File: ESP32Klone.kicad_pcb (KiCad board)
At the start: 2 copper layers, 52.1 x 65.5 mm, 23 parts, among them J1 USB_C_Receptacle_USB2.0_14P, J2 Conn_01x14_Socket, J3 Conn_01x14_Socket, U1 CH340G, U2 AMS1117-3.3, U3 ESP32-WROOM-32E, X1 12MHz

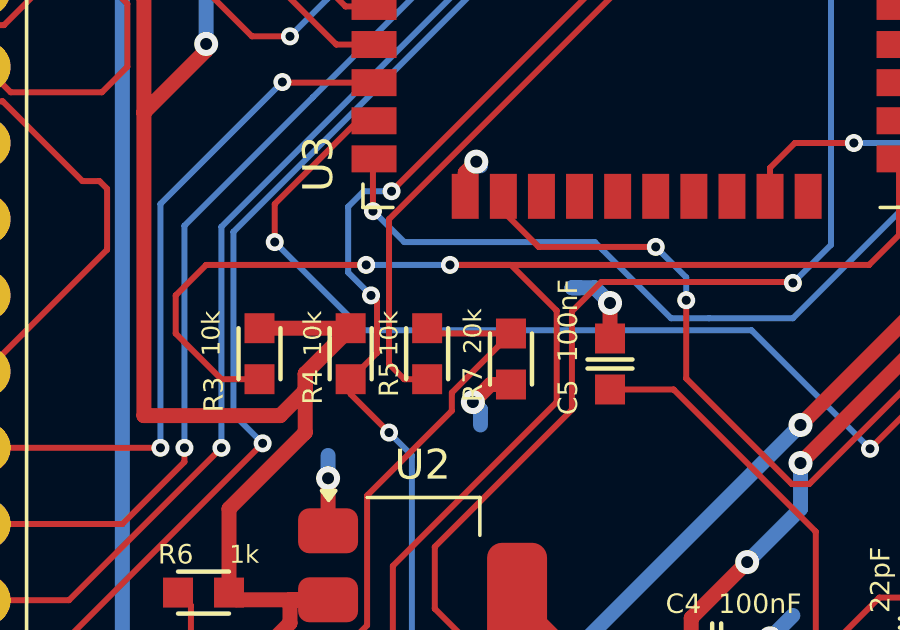
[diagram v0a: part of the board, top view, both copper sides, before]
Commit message: fix: correct UART Rx level shifter wiring (R5/R7)
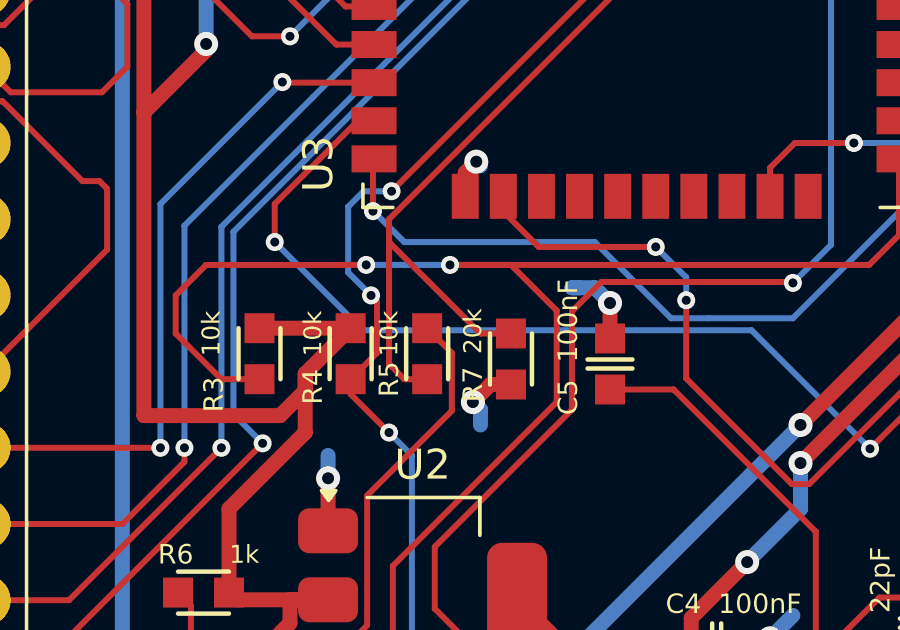
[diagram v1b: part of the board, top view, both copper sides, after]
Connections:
- R7 pad 1: /TXD/RXD -> Net-(U3-RXD0/IO3)
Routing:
- net Net-(U3-RXD0/IO3): track 28.9 -> 34.2 mm
- net /TXD/RXD: track 80.5 -> 77.3 mm
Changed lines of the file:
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@@
 			(size 1 1)
 			(layers "F.Cu" "F.Mask" "F.Paste")
-			(net 39 "/TXD{slash}RXD")
+			(net 38 "Net-(U3-RXD0{slash}IO3)")
 			(pintype "passive")
 		)
@@
 	)
 	(segment
+		(start 141.732 106.934)
+		(end 140.716 106.934)
+		(width 0.2)
+		(layer "F.Cu")
+		(net 38)
+	)
+	(segment
 		(start 145.542 95.25)
 		(end 147.574 95.25)
@@
 	)
 	(segment
+		(start 137.668 107.95)
+		(end 137.668 103.886)
+		(width 0.2)
+		(layer "F.Cu")
+		(net 38)
+	)
+	(segment
 		(start 138.176 108.458)
 		(end 137.668 107.95)
@@
 	)
 	(segment
-		(start 137.668 107.95)
-		(end 137.668 103.124)
+		(start 140.716 106.934)
+		(end 137.668 103.886)
 		(width 0.2)
 		(layer "F.Cu")
@@
 	)
 	(segment
-		(start 147.574 95.25)
-		(end 153.142 89.682)
+		(start 137.668 103.886)
+		(end 137.668 103.124)
 		(width 0.2)
 		(layer "F.Cu")
@@
 	)
 	(segment
-		(start 153.269 126.731968)
-		(end 153.269 126.445101)
+		(start 147.574 95.25)
+		(end 153.142 89.682)
 		(width 0.2)
 		(layer "F.Cu")
-		(net 39)
+		(net 38)
 	)
 	(segment
-		(start 151.476968 128.524)
-		(end 153.269 126.731968)
+		(start 136.974215 136.291)
+		(end 134.335 133.651785)
 		(width 0.2)
 		(layer "F.Cu")
@@
 	)
 	(segment
-		(start 149.854 123.103032)
-		(end 150.114032 122.843)
+		(start 154.833 134.7861)
+		(end 153.3281 136.291)
 		(width 0.2)
 		(layer "F.Cu")
@@
 	)
 	(segment
-		(start 153.3281 136.291)
-		(end 136.974215 136.291)
+		(start 154.833 125.530032)
+		(end 154.833 134.7861)
 		(width 0.2)
 		(layer "F.Cu")
@@
 	)
 	(segment
-		(start 150.114032 122.843)
-		(end 152.145968 122.843)
+		(start 153.269 126.731968)
+		(end 153.269 126.445101)
 		(width 0.2)
 		(layer "F.Cu")
@@
 	)
 	(segment
-		(start 136.937 112.334364)
-		(end 139.761 109.510364)
+		(start 136.937 116.663008)
+		(end 136.937 112.334364)
 		(width 0.2)
 		(layer "F.Cu")
@@
 	)
 	(segment
-		(start 139.761 108.905)
-		(end 141.732 106.934)
+		(start 152.145968 122.843)
+		(end 154.833 125.530032)
 		(width 0.2)
 		(layer "F.Cu")
@@
 	)
 	(segment
-		(start 136.937 116.663008)
-		(end 136.937 112.334364)
+		(start 150.114032 122.843)
+		(end 152.145968 122.843)
 		(width 0.2)
 		(layer "F.Cu")
@@
 	)
 	(segment
-		(start 139.761 109.510364)
-		(end 139.761 108.905)
+		(start 149.854 123.103032)
+		(end 150.114032 122.843)
 		(width 0.2)
 		(layer "F.Cu")
@@
 	)
 	(segment
-		(start 149.854 125.054968)
-		(end 149.854 123.103032)
+		(start 152.138899 125.315)
+		(end 150.114032 125.315)
 		(width 0.2)
 		(layer "F.Cu")
@@
 	)
 	(segment
-		(start 134.335 117.454992)
-		(end 134.730992 117.059)
+		(start 139.761 107.581)
+		(end 138.938 106.758)
 		(width 0.2)
 		(layer "F.Cu")
@@
 	)
 	(segment
-		(start 151.13 128.524)
-		(end 151.476968 128.524)
+		(start 149.854 125.054968)
+		(end 149.854 123.103032)
 		(width 0.2)
 		(layer "F.Cu")
@@
 	)
 	(segment
-		(start 152.138899 125.315)
-		(end 150.114032 125.315)
+		(start 134.335 133.651785)
+		(end 134.335 117.454992)
 		(width 0.2)
 		(layer "F.Cu")
@@
 	)
 	(segment
-		(start 154.833 125.530032)
-		(end 154.833 134.7861)
+		(start 136.937 112.334364)
+		(end 139.761 109.510364)
 		(width 0.2)
 		(layer "F.Cu")
@@
 	)
 	(segment
-		(start 141.732 106.934)
-		(end 139.114 106.934)
+		(start 151.476968 128.524)
+		(end 153.269 126.731968)
 		(width 0.2)
 		(layer "F.Cu")
@@
 	)
 	(segment
-		(start 154.833 134.7861)
-		(end 153.3281 136.291)
+		(start 153.3281 136.291)
+		(end 136.974215 136.291)
 		(width 0.2)
 		(layer "F.Cu")
@@
 	)
 	(segment
-		(start 134.730992 117.059)
-		(end 136.541008 117.059)
+		(start 134.335 117.454992)
+		(end 134.730992 117.059)
 		(width 0.2)
 		(layer "F.Cu")
@@
 	)
 	(segment
-		(start 150.114032 125.315)
-		(end 149.854 125.054968)
+		(start 151.13 128.524)
+		(end 151.476968 128.524)
 		(width 0.2)
 		(layer "F.Cu")
@@
 	)
 	(segment
-		(start 139.114 106.934)
-		(end 138.938 106.758)
+		(start 153.269 126.445101)
+		(end 152.138899 125.315)
 		(width 0.2)
 		(layer "F.Cu")
@@
 	)
 	(segment
-		(start 152.145968 122.843)
-		(end 154.833 125.530032)
-		(width 0.2)
-		(layer "F.Cu")
-		(net 39)
-	)
-	(segment
-		(start 153.269 126.445101)
-		(end 152.138899 125.315)
+		(start 150.114032 125.315)
+		(end 149.854 125.054968)
 		(width 0.2)
 		(layer "F.Cu")
@@
 	)
 	(segment
-		(start 134.335 133.651785)
-		(end 134.335 117.454992)
+		(start 134.730992 117.059)
+		(end 136.541008 117.059)
 		(width 0.2)
 		(layer "F.Cu")
@@
 	)
 	(segment
-		(start 136.974215 136.291)
-		(end 134.335 133.651785)
+		(start 139.761 109.510364)
+		(end 139.761 107.581)
 		(width 0.2)
 		(layer "F.Cu")

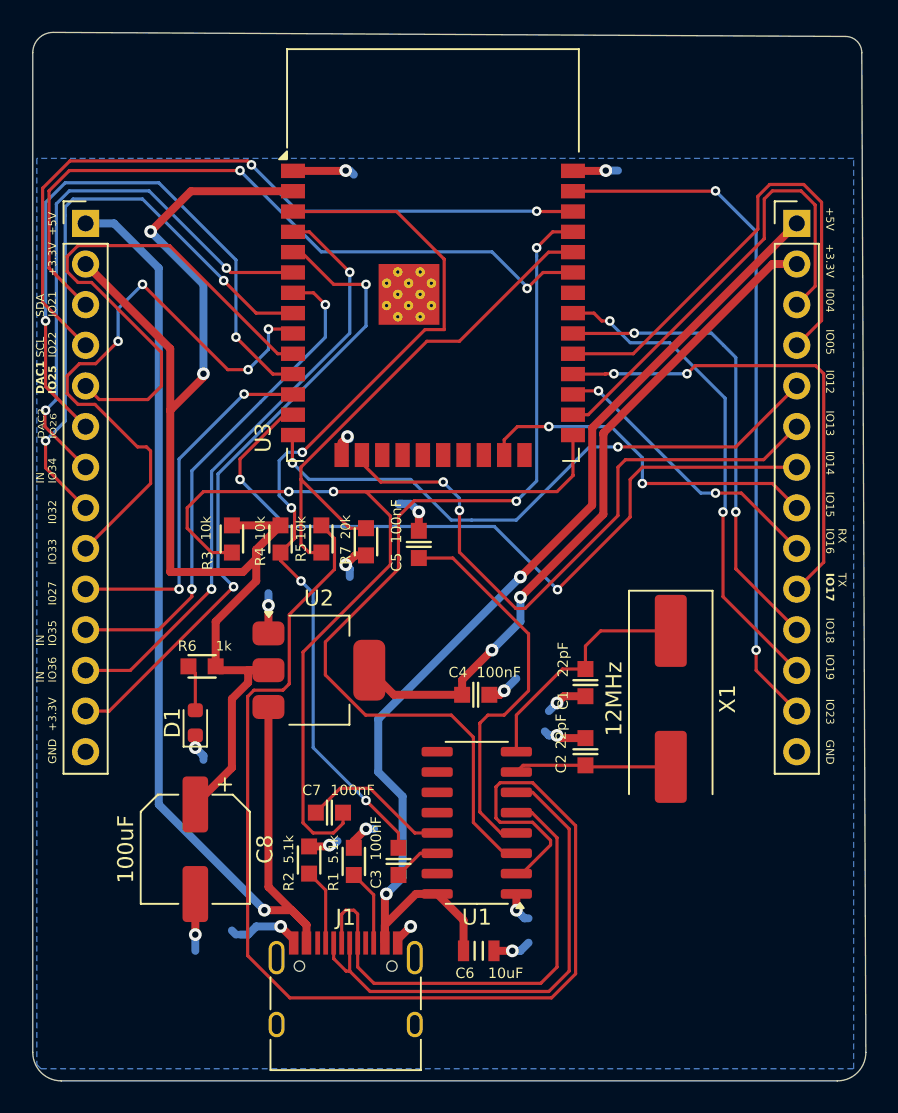
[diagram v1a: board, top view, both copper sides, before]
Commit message: Added F.Cu copperfill
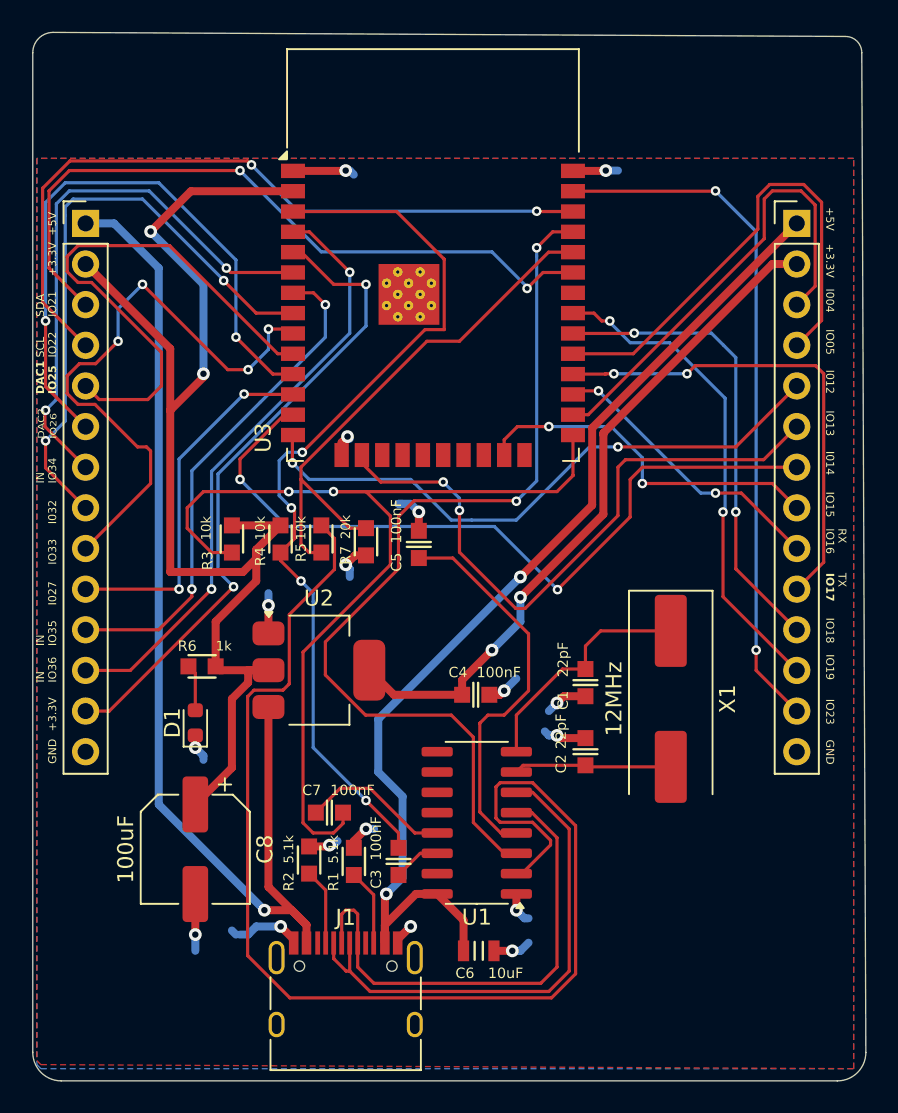
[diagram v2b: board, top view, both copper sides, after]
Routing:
- added copper zone on F.Cu, net GND
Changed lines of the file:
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@@
+		(net 2)
+		(net_name "GND")
+		(layer "F.Cu")
+		(hatch edge 0.5)
+		(priority 1)
+		(connect_pads
+			(clearance 0.5)
+		)
+		(min_thickness 0.25)
+		(filled_areas_thickness no)
+		(fill yes
+			(thermal_gap 0.5)
+			(thermal_bridge_width 0.5)
+		)
+		(polygon
+			(pts
+				(xy 121.412 140.462) (xy 172.212 140.716) (xy 172.212 83.82) (xy 121.158 83.82) (xy 121.158 140.208)
+			)
+		)
+	)
+	(zone
 		(net 2)
 		(net_name "GND")

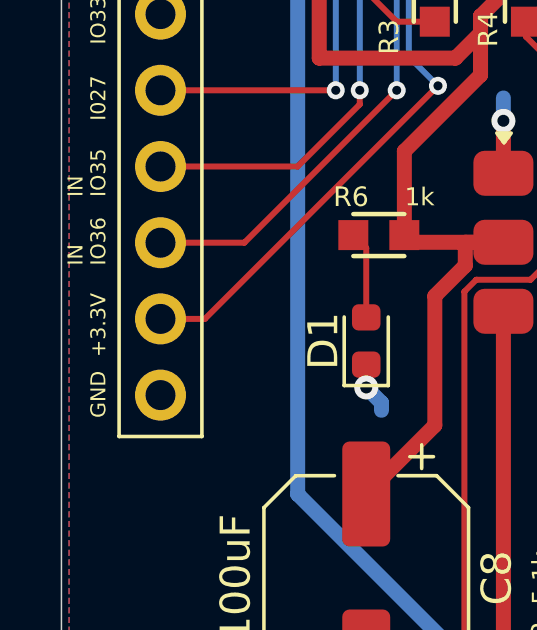
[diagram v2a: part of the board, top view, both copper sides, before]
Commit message: fix: silkscreen GPIO39 label corrected
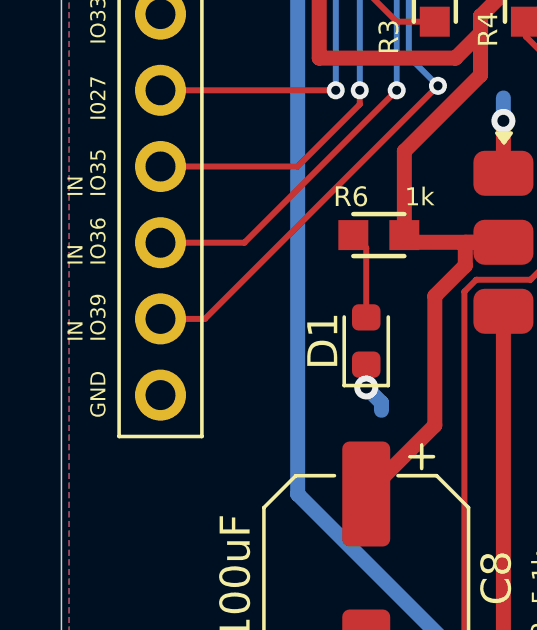
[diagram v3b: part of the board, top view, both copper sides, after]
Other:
- board text added: "IO39"
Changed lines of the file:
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@@
 		)
 	)
-	(gr_text "+3.3V"
-		(at 122.428 119.634 90)
+	(gr_text "IO39\n"
+		(at 122.428 119.126 90)
 		(layer "F.SilkS")
 		(effects
@@
 		(layer "F.SilkS")
 		(effects
+			(font
+				(size 0.5 0.5)
+				(thickness 0.1)
+			)
+			(justify left bottom)
+		)
+	)
+	(gr_text "IN"
+		(at 121.666 119.126 90)
+		(layer "F.SilkS")
+		(effects
